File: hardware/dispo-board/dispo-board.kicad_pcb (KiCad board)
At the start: 4 copper layers, 84.3 x 56.4 mm, 103 parts, among them J1 Conn_01x03, J10 Conn_01x02, J11 Conn_01x02, J12 Conn_01x03, J13 Conn_01x03, J14 Conn_ARM_JTAG_SWD_10, J2 Conn_01x03, J3 Conn_01x03, J4 Conn_01x04, J5 USB_B_Micro, J6 Conn_01x02, J7 Conn_01x02, J8 Conn_01x02, J9 Conn_01x02, SW1 SW_Push, U1 TPS79633DCQ, U2 STM32H725RGV6, U3 OPA1671, U4 CS5343-CZZ, U5 OPA1671, U6 CS4344-CZZR, Y1 32M

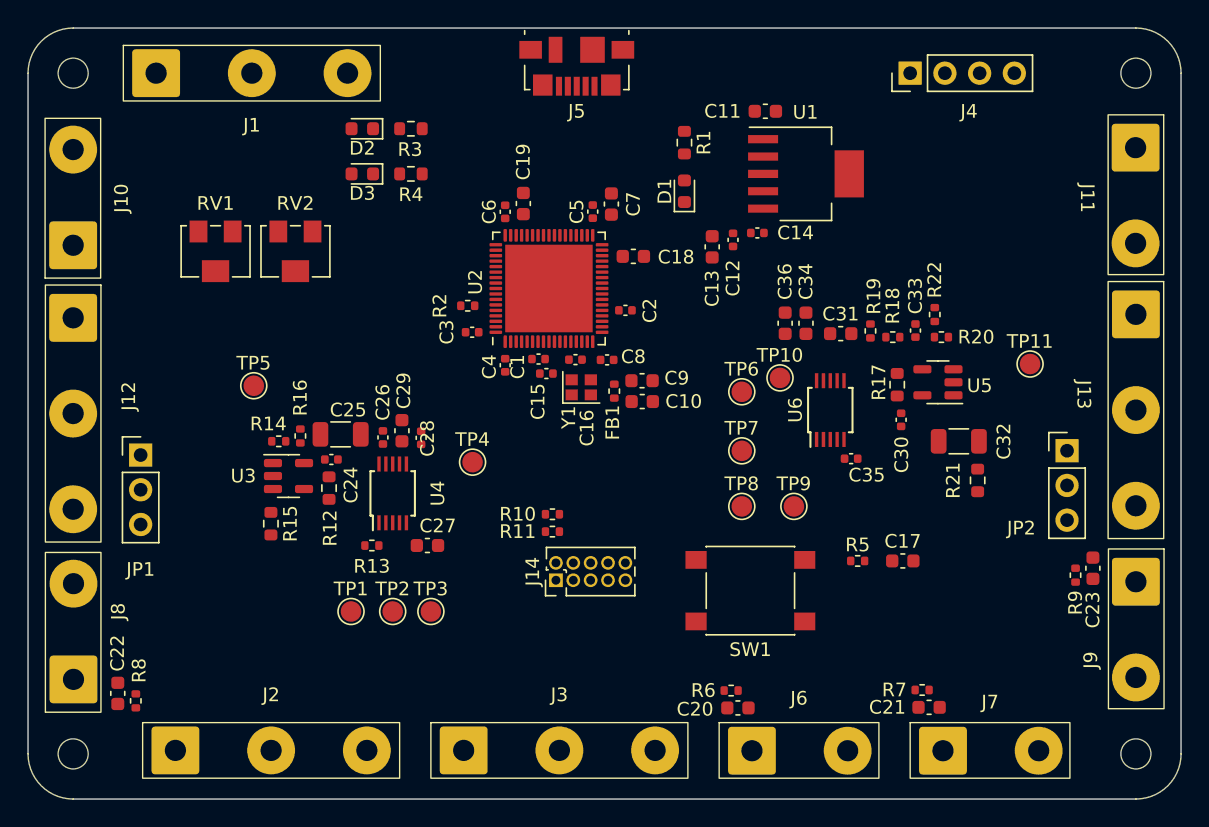
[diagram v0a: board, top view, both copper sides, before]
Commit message: pcb layout drc check passed
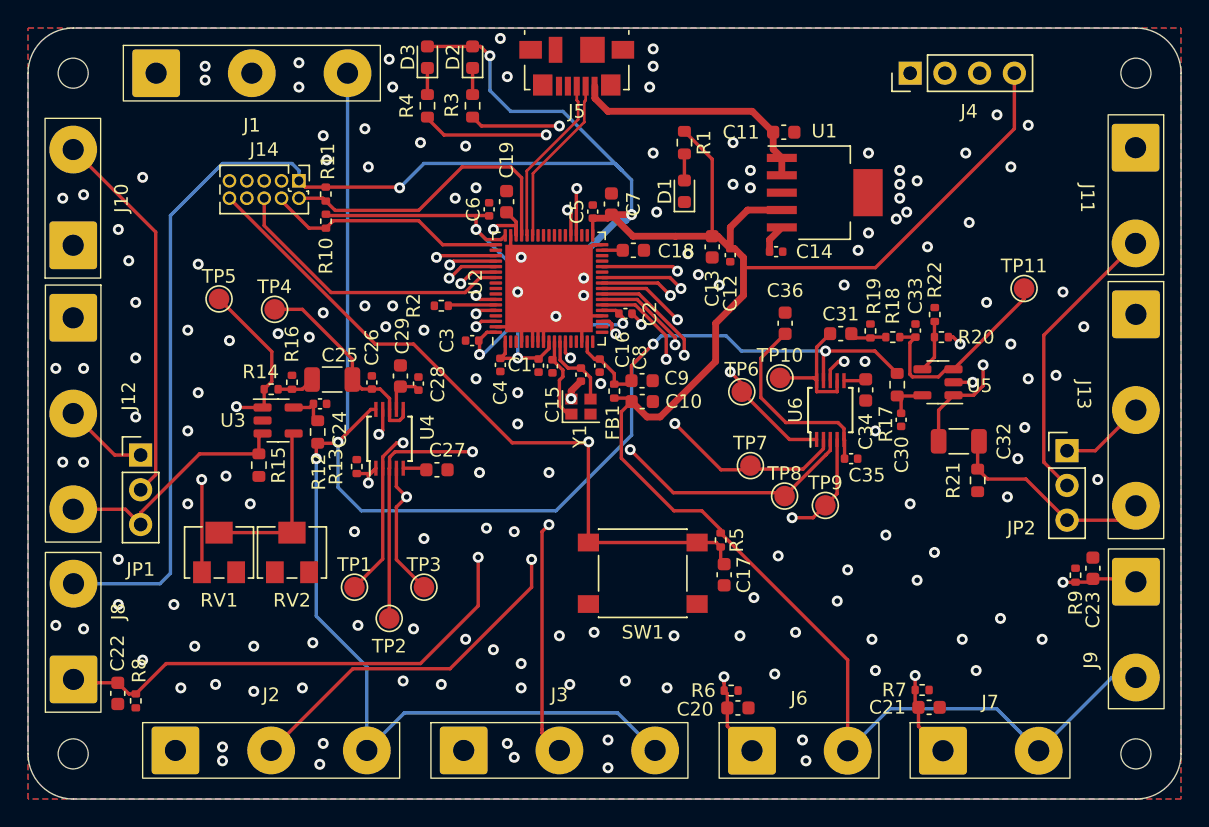
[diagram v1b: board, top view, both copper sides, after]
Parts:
- moved J14 34.7 mm to (46.0, 33.3), turned to -90 degrees
- moved R11 29.7 mm to (47.9, 34.2), turned to -90 degrees
- moved R10 27.1 mm to (48.0, 36.2), turned to -90 degrees
- moved RV1 22.0 mm to (40.1, 60.5), turned to 180 degrees
- moved RV2 22.0 mm to (45.5, 60.5), turned to 180 degrees
- moved TP4 18.3 mm to (44.2, 42.7)
- moved C17 13.1 mm to (77.1, 62.1), turned to -90 degrees
- moved R5 10.1 mm to (76.8, 59.5), turned to -90 degrees
- moved D3 9.77 mm to (55.4, 24.2), turned to 90 degrees
- moved D2 9.61 mm to (58.7, 24.2), turned to 90 degrees
- moved SW1 7.98 mm to (71.1, 62.0)
- moved TP5 6.84 mm to (40.1, 41.9)
- moved C34 6.55 mm to (87.4, 48.6), turned to -90 degrees
- moved R13 5.88 mm to (50.2, 54.2), turned to -90 degrees
- moved C27 5.58 mm to (56.1, 54.4)
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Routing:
- net +3V3: track 0.00 -> 286.7 mm, vias 0 -> 7
- net +3.3VA: track 0.00 -> 145.5 mm, vias 0 -> 4
- net GUITAR_bypass: track 0.00 -> 108.4 mm
- net DIG_IN4: track 0.00 -> 76.5 mm, vias 0 -> 2
- net DIG_IN2: track 0.00 -> 68.9 mm, vias 0 -> 2
- net I2S6_MCK: track 0.00 -> 65.1 mm, vias 0 -> 3
- net ADC1_INP5: track 0.00 -> 63.2 mm, vias 0 -> 2
- net I2S6_WS: track 0.00 -> 63.0 mm, vias 0 -> 3
- net DIG_IN3: track 0.00 -> 61.5 mm, vias 0 -> 2
- net NRST: track 0.00 -> 61.5 mm, vias 0 -> 2
- net I2S6_CK: track 0.00 -> 60.7 mm, vias 0 -> 3
- net DIG_IN1: track 0.00 -> 56.4 mm, vias 0 -> 2
- net GND: track 0.00 -> 50.7 mm, vias 0 -> 157
- net ADC1_INP8: track 0.00 -> 50.3 mm, vias 0 -> 2
- net I2C1_SCL: track 0.00 -> 47.6 mm, vias 0 -> 1
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- added copper zone on B.Cu, net GND
- added copper zone on F.Cu, net GND

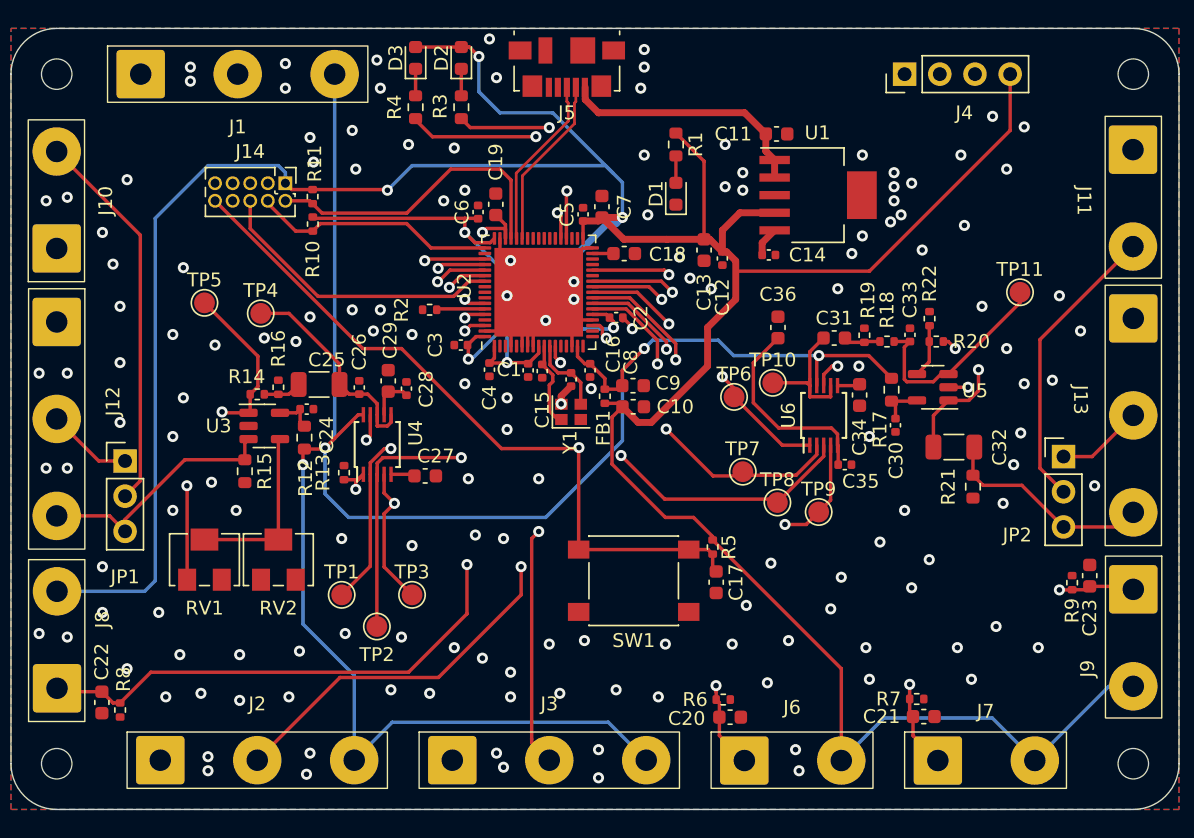
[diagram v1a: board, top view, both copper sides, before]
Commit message: corrected vias and placements
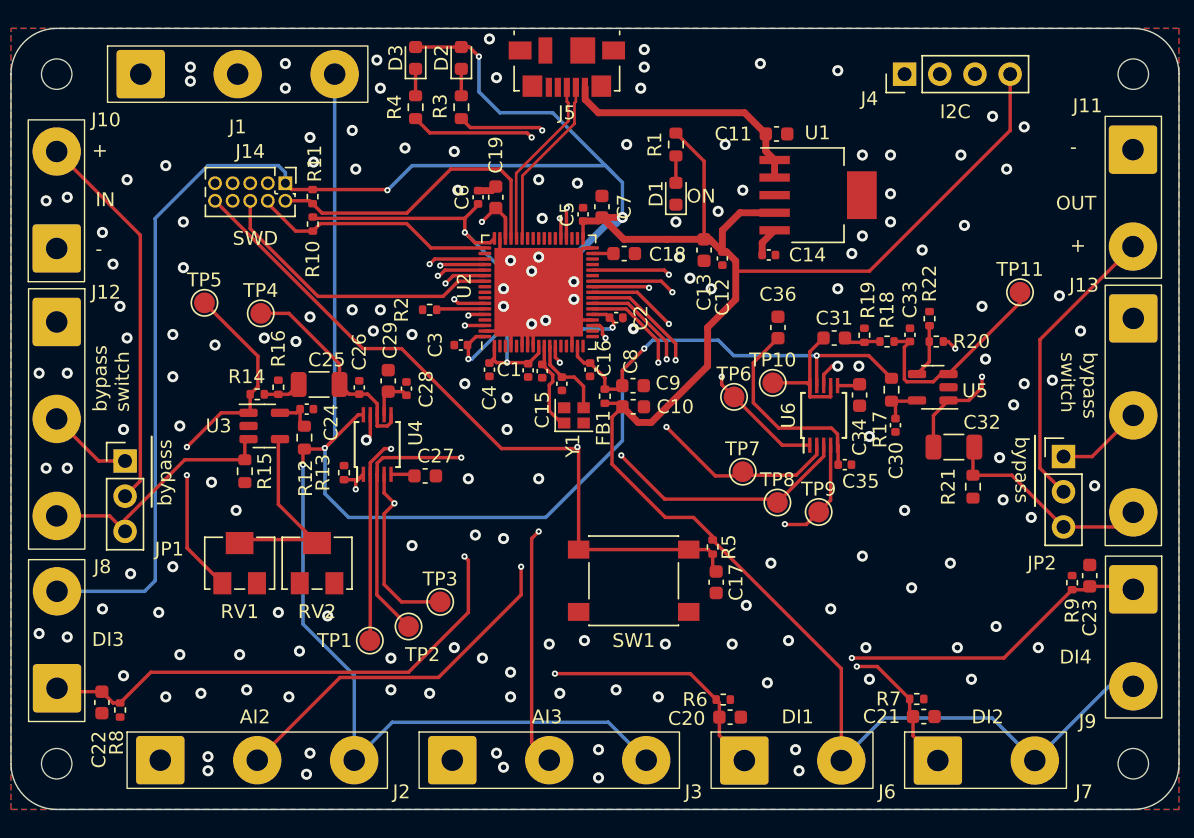
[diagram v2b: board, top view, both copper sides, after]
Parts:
- added G***: LOGO, MyFootprints:own-logo, B.Cu at (96.0, 33.3)
- moved TP1 3.88 mm to (52.1, 66.3)
- moved RV2 2.81 mm to (48.3, 60.7)
- moved RV1 2.55 mm to (42.7, 60.7)
- moved TP2 2.29 mm to (54.9, 65.3)
- moved TP3 2.09 mm to (57.1, 63.5)
- moved C6 1.07 mm to (59.9, 34.3)
- moved C16 0.73 mm to (65.9, 47.8)
- moved C19 0.51 mm to (61.2, 34.3)
- moved Y1 0.33 mm to (66.8, 50.0)
- moved C8 0.05 mm to (68.0, 46.7)
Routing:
- net I2S6_MCK: track 65.1 -> 67.9 mm
- net GND: track 50.7 -> 48.0 mm, vias 157 -> 160
- net ADC1_INP4: track 46.9 -> 44.5 mm
- net I2S6_CK: track 60.7 -> 63.0 mm
- net Net-(U3--): track 12.6 -> 14.5 mm
- net Net-(U3-OUT): track 24.9 -> 26.2 mm
- net I2C1_SDA: track 43.8 -> 44.9 mm
- net DIG_IN1: track 56.4 -> 55.5 mm
- net I2S6_WS: track 63.0 -> 63.9 mm
- net Net-(C19-Pad1): track 18.4 -> 19.3 mm
- net DIG_IN2: track 68.9 -> 68.2 mm
- net I2S6_SDO: track 20.6 -> 21.2 mm
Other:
- board text added: "+"
- board text added: "-"
- board text added: "AI2"
- board text added: "AI3"
- board text added: "DI1"
- board text added: "DI2"
- board text added: "DI3"
- board text added: "DI4"
- board text added: "I2C"
- board text added: "IN"
- board text added: "ON"
- board text added: "OUT"
- board text added: "SWD"
- board text added: "bypass"
- board text added: "bypass switch"

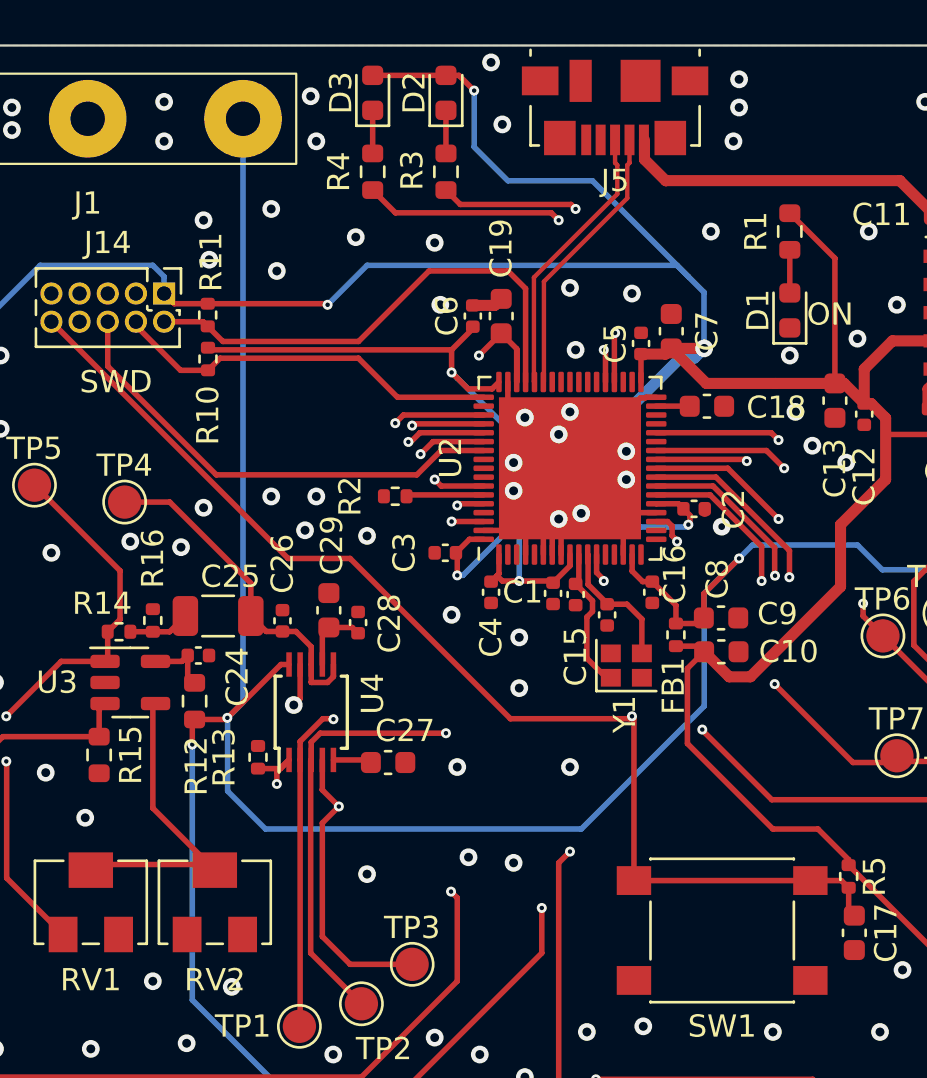
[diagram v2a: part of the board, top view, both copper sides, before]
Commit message: updated pcb, changed via sizes, drc check, ...
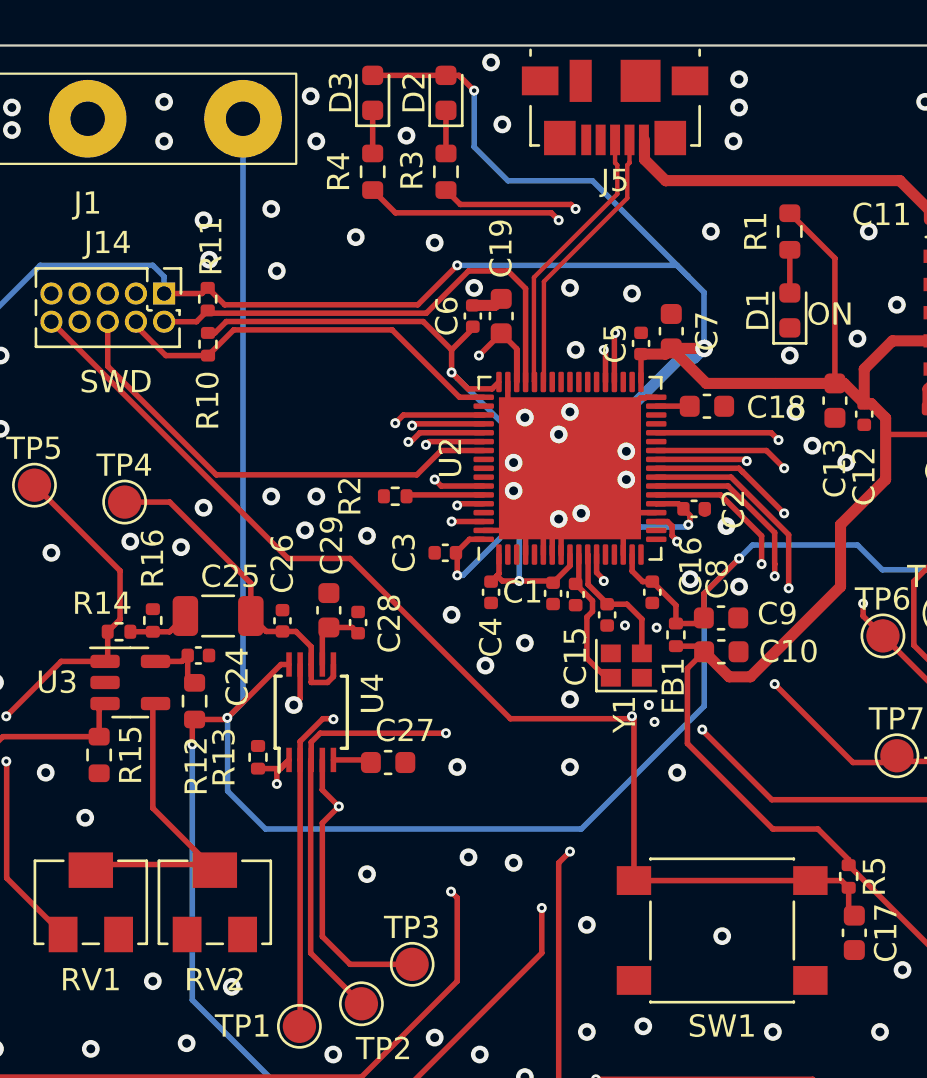
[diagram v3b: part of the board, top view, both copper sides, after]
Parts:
- moved R11 0.72 mm to (47.9, 33.5)
- moved R10 0.66 mm to (48.0, 35.6)
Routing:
- net +3V3: track 287.0 -> 287.9 mm
- net SWDIO: track 22.5 -> 21.9 mm
- net SWCLK: track 17.6 -> 18.1 mm
- net GND: vias 160 -> 171
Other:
- board text added: "dispo V1.0"
